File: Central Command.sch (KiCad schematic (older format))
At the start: 19 parts, among them P1 CONN_01X06, P2 CONN_01X02, U1 STM32F030C8, U2 MCP1700T-3302E/TT_, Y1 Crystal

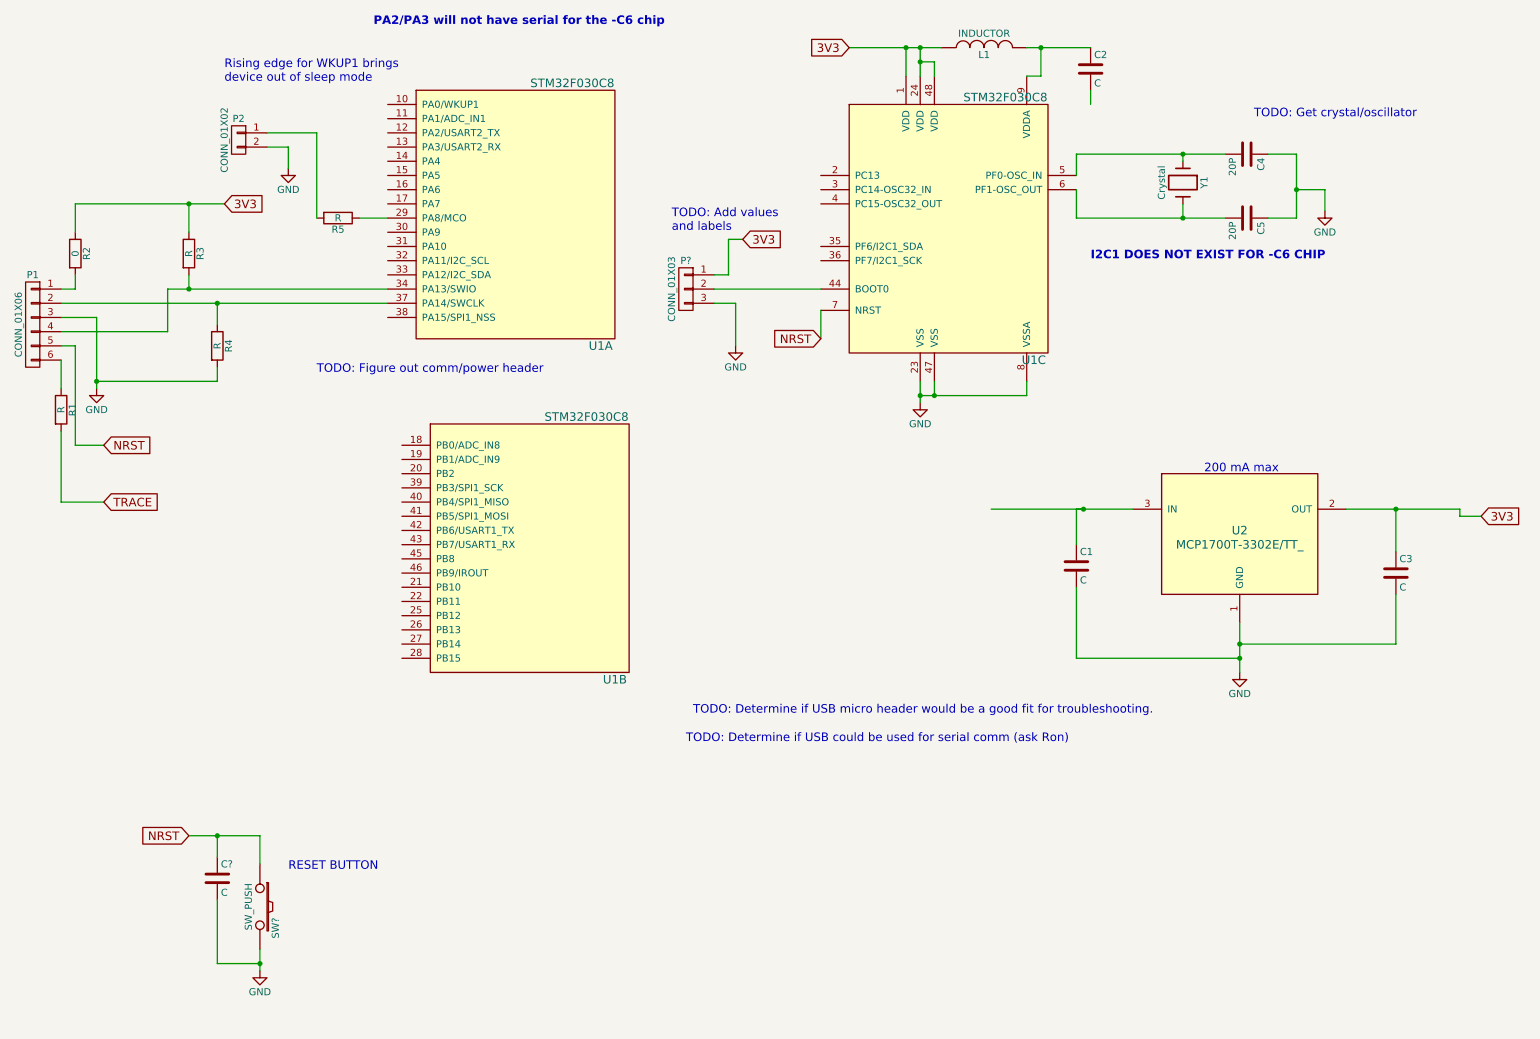
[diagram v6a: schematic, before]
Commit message: Added a USB to serial section
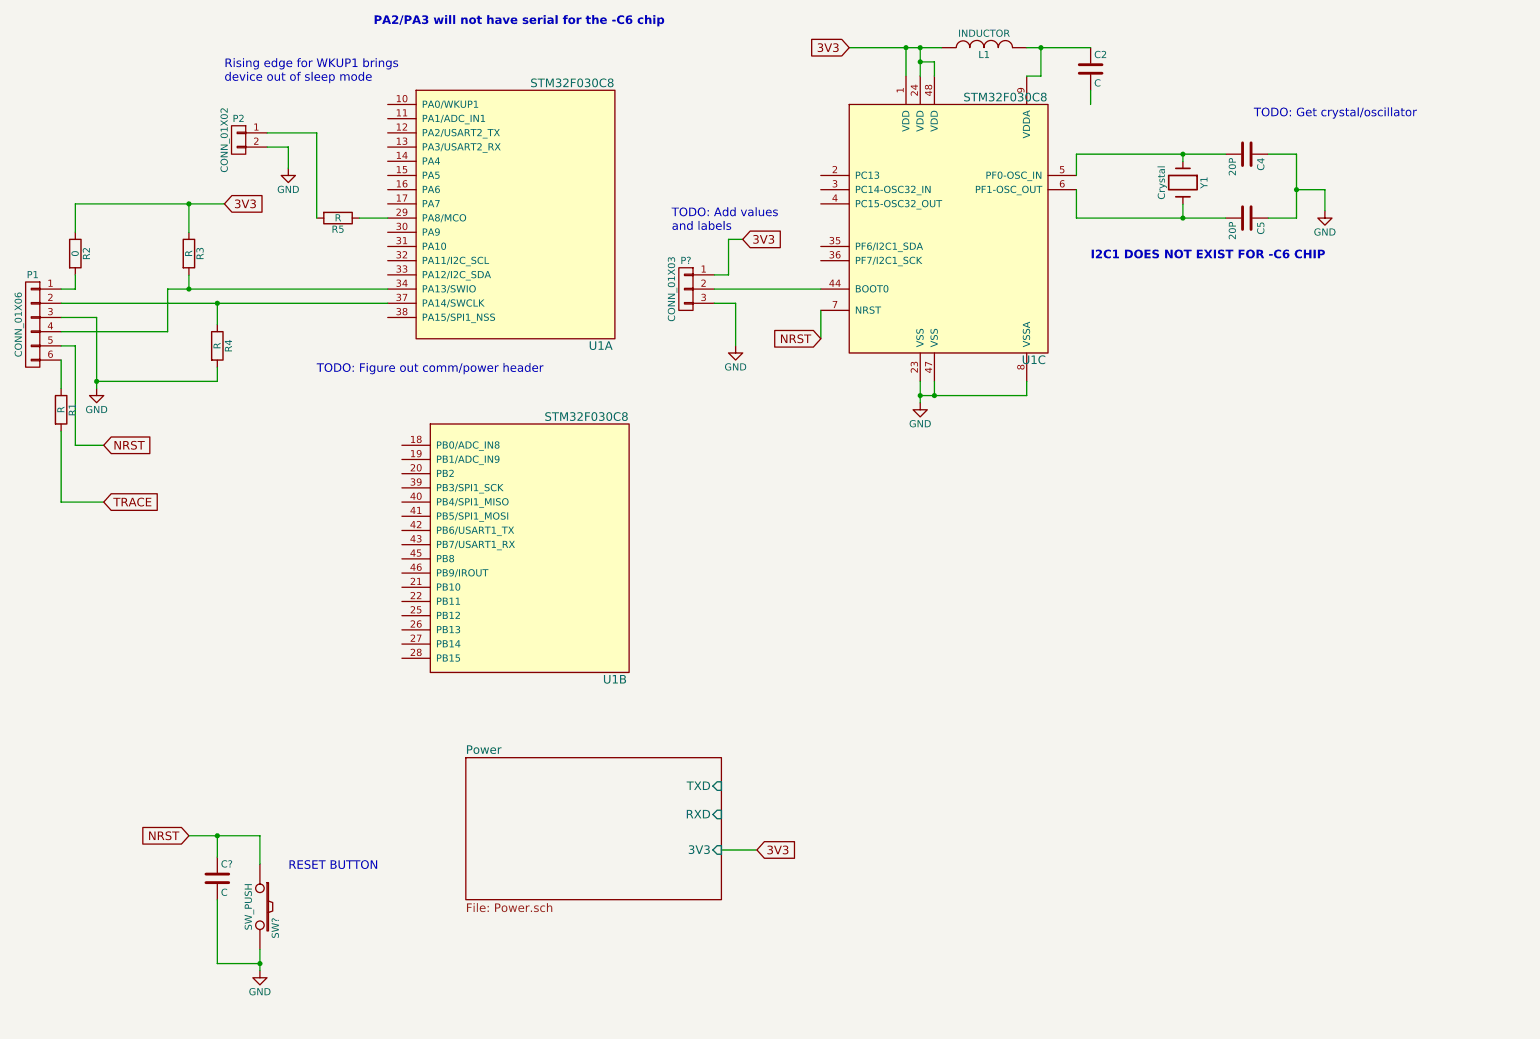
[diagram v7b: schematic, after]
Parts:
- removed C1, C3: C, Capacitors_SMD:C_0805, symbol C
- removed U2: MCP1700T-3302E/TT_, Housings_SOT-23_SOT-143_TSOT-6:SOT-23, symbol MCP1700T-3302E/TT_
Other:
- note removed: "200 mA max"
- note removed: "TODO: Determine if USB could be used for serial comm (ask Ron)"
- note removed: "TODO: Determine if USB micro header would be a good fit for troubleshooting."
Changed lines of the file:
@@
 $Descr A4 11693 8268
 encoding utf-8
-Sheet 1 1
+Sheet 1 2
 Title ""
 Date ""
@@
 	1    0    0    -1
 $EndComp
-$Comp
-L MCP1700T-3302E/TT_ U2
-U 1 1 56270053
-P 9050 4200
-F 0 "U2" H 9050 4200 60  0000 C CNN
-F 1 "MCP1700T-3302E/TT_" H 9050 4100 60  0000 C CNN
-F 2 "Housings_SOT-23_SOT-143_TSOT-6:SOT-23" H 9050 4200 60  0001 C CNN
-F 3 "" H 9050 4200 60  0000 C CNN
-F 4 "http://parts.io/detail/1370896/MCP1700T-3302E%2FTT" H 9050 4200 60  0001 C CNN "Link"
-	1    9050 4200
-	1    0    0    -1
-$EndComp
-$Comp
-L C C1
-U 1 1 5627009A
-P 7900 4450
-F 0 "C1" H 7925 4550 50  0000 L CNN
-F 1 "C" H 7925 4350 50  0000 L CNN
-F 2 "Capacitors_SMD:C_0805" H 7938 4300 30  0001 C CNN
-F 3 "" H 7900 4450 60  0000 C CNN
-	1    7900 4450
-	1    0    0    -1
-$EndComp
-$Comp
-L C C3
-U 1 1 56270119
-P 10150 4500
-F 0 "C3" H 10175 4600 50  0000 L CNN
-F 1 "C" H 10175 4400 50  0000 L CNN
-F 2 "Capacitors_SMD:C_0805" H 10188 4350 30  0001 C CNN
-F 3 "" H 10150 4500 60  0000 C CNN
-	1    10150 4500
-	1    0    0    -1
-$EndComp
-$Comp
-L GND #PWR01
-U 1 1 562701EB
-P 9050 5200
-F 0 "#PWR01" H 9050 4950 50  0001 C CNN
-F 1 "GND" H 9050 5050 50  0000 C CNN
-F 2 "" H 9050 5200 60  0000 C CNN
-F 3 "" H 9050 5200 60  0000 C CNN
-	1    9050 5200
-	1    0    0    -1
-$EndComp
-Text GLabel 10750 4100 2    60   Input ~ 0
-3V3
 Text GLabel 6300 800  0    60   Input ~ 0
 3V3
@@
 	1    0    0    -1
 $EndComp
-Text Notes 8800 3800 0    60   ~ 0
-200 mA max
 $Comp
 L CONN_01X06 P1
@@
 Text Notes 2550 3100 0    60   ~ 0
 TODO: Figure out comm/power header
-Text Notes 5200 5500 0    60   ~ 0
-TODO: Determine if USB micro header would be a good fit for troubleshooting.
-Text Notes 5150 5700 0    60   ~ 0
-TODO: Determine if USB could be used for serial comm (ask Ron)
 $Comp
 L Crystal Y1
@@
 	6900 900  6800 900
 Connection ~ 6800 900
-Wire Wire Line
-	9050 4850 9050 5200
-Wire Wire Line
-	9050 5000 10150 5000
-Wire Wire Line
-	10150 5000 10150 4650
-Connection ~ 9050 5000
-Wire Wire Line
-	9050 5100 7900 5100
-Wire Wire Line
-	7900 5100 7900 4600
-Connection ~ 9050 5100
-Wire Wire Line
-	7300 4050 8300 4050
-Wire Wire Line
-	7900 4300 7900 4050
-Wire Wire Line
-	7900 4050 7950 4050
-Connection ~ 7950 4050
-Wire Wire Line
-	9800 4050 10600 4050
-Wire Wire Line
-	10150 4050 10150 4350
-Connection ~ 10150 4050
-Wire Wire Line
-	10750 4100 10600 4100
-Wire Wire Line
-	10600 4100 10600 4050
 Connection ~ 6700 800
 Wire Wire Line
@@
 Text Notes 1900 1050 0    60   ~ 0
 Rising edge for WKUP1 brings \ndevice out of sleep mode
+$Sheet
+S 3600 5800 1800 1000
+U 56440BA6
+F0 "Power" 60
+F1 "Power.sch" 60
+F2 "TXD" I R 5400 6000 60
+F3 "RXD" I R 5400 6200 60
+F4 "3V3" I R 5400 6450 60
+$EndSheet
+Text GLabel 5650 6450 2    60   Input ~ 0
+3V3
+Wire Wire Line
+	5650 6450 5400 6450
 $EndSCHEMATC

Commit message: Added headers and created a new sheet for communication headers
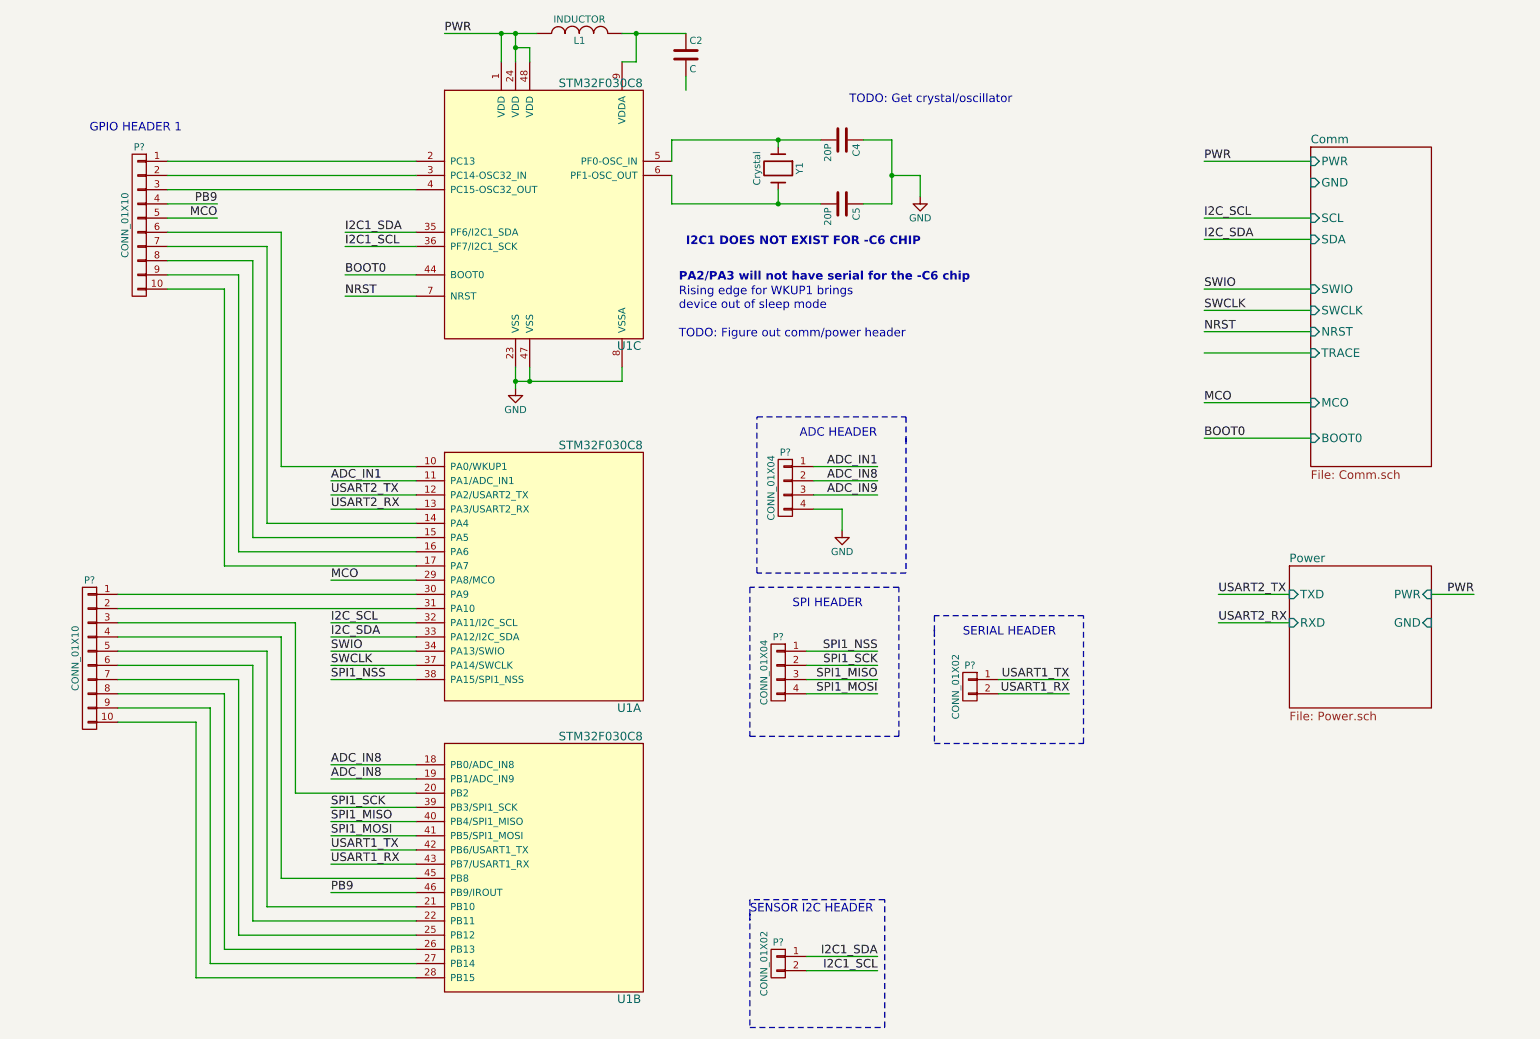
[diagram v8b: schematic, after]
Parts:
- removed C?: C, symbol C
- removed P1: CONN_01X06, Pin_Headers:Pin_Header_Straight_1x06, symbol CONN_01X06
- removed P2: CONN_01X02, Pin_Headers:Pin_Header_Straight_1x02, symbol CONN_01X02
- removed P?: CONN_01X03, symbol CONN_01X03
- removed R1, R3, R4, R5: R, Resistors_SMD:R_0805, symbol R
- removed R2: 0, Resistors_SMD:R_0805, symbol R
- removed SW?: SW_PUSH, symbol SW_PUSH
- added P? (x2): CONN_01X10, symbol CONN_01X10
- added P? (x2): CONN_01X04, symbol CONN_01X04
- added P? (x2): CONN_01X02, symbol CONN_01X02
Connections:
- net GND: now also P?.4 (P4)
- net SWCLK: now reaches U1.37 (PA14/SWCLK)
- net SWIO: now reaches U1.34 (PA13/SWIO)
- net MCO: now reaches U1.29 (PA8/MCO)
- net MCO: now also P?.5 (P5)
- net at U1.10 (PA0/WKUP1): now also P?.6 (P6)
- net ADC_IN1: now reaches U1.11 (PA1/ADC_IN1)
- net ADC_IN1: now also P?.1 (P1)
- net USART2_TX: now reaches U1.12 (PA2/USART2_TX)
- net USART2_RX: now reaches U1.13 (PA3/USART2_RX)
- net at U1.14 (PA4): now also P?.7 (P7)
- net at U1.15 (PA5): now also P?.8 (P8)
- net at U1.16 (PA6): now also P?.9 (P9)
- net at U1.17 (PA7): now also P?.10 (P10)
- net at U1.30 (PA9): now also P?.1 (P1)
- net at U1.31 (PA10): now also P?.2 (P2)
- net I2C_SCL: now reaches U1.32 (PA11/I2C_SCL)
- net I2C_SDA: now reaches U1.33 (PA12/I2C_SDA)
- net SPI1_NSS: now reaches U1.38 (PA15/SPI1_NSS)
- net SPI1_NSS: now also P?.1 (P1)
- net ADC_IN8: now reaches U1.18 (PB0/ADC_IN8)
- net ADC_IN8: now also U1.19 (PB1/ADC_IN9), P?.2 (P2)
- net at U1.20 (PB2): now also P?.3 (P3)
- net at U1.21 (PB10): now also P?.5 (P5)
- net at U1.22 (PB11): now also P?.6 (P6)
- net at U1.25 (PB12): now also P?.7 (P7)
- net at U1.26 (PB13): now also P?.8 (P8)
- net at U1.27 (PB14): now also P?.9 (P9)
- net at U1.28 (PB15): now also P?.10 (P10)
- net SPI1_SCK: now reaches U1.39 (PB3/SPI1_SCK)
- net SPI1_SCK: now also P?.2 (P2)
- net SPI1_MISO: now reaches U1.40 (PB4/SPI1_MISO)
- net SPI1_MISO: now also P?.3 (P3)
- net SPI1_MOSI: now reaches U1.41 (PB5/SPI1_MOSI)
- net SPI1_MOSI: now also P?.4 (P4)
- net USART1_TX: now reaches U1.42 (PB6/USART1_TX)
- net USART1_TX: now also P?.1 (P1)
- net USART1_RX: now reaches U1.43 (PB7/USART1_RX)
- net USART1_RX: now also P?.2 (P2)
- net at U1.45 (PB8): now also P?.4 (P4)
- net PB9: now reaches U1.46 (PB9/IROUT)
- net PB9: now also P?.4 (P4)
- net at U1.2 (PC13): now also P?.1 (P1)
- net at U1.3 (PC14-OSC32_IN): now also P?.2 (P2)
- net I2C1_SDA: now reaches U1.35 (PF6/I2C1_SDA)
- net I2C1_SDA: now also P?.1 (P1)
- net I2C1_SCL: now reaches U1.36 (PF7/I2C1_SCK)
- net I2C1_SCL: now also P?.2 (P2)
- net at U1.4 (PC15-OSC32_OUT): now also P?.3 (P3)
- net BOOT0: now reaches U1.44 (BOOT0)
- net 3V3 renamed PWR
- new net ADC_IN9: P?.3 (P3)
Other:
- note added: "ADC HEADER"
- note added: "GPIO HEADER 1"
- note added: "SENSOR I2C HEADER"
- note added: "SERIAL HEADER"
- note added: "SPI HEADER"
- note removed: "RESET BUTTON"
- note removed: "TODO: Add values \nand labels"
- moved on the sheet: C2, C4, C5, L1, U1A, U1B, U1C, Y1
